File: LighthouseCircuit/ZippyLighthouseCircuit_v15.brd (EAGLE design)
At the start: 25.4 x 8.9 mm, 23 parts

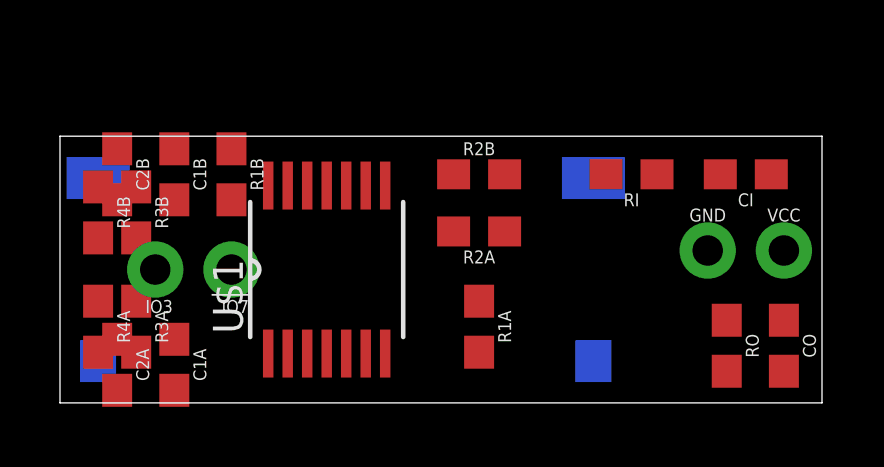
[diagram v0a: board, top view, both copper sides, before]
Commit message: Significant changes and refactored codebase layout. Improvements made to path following, PID control, path execution, added a new default path, and many other changes.
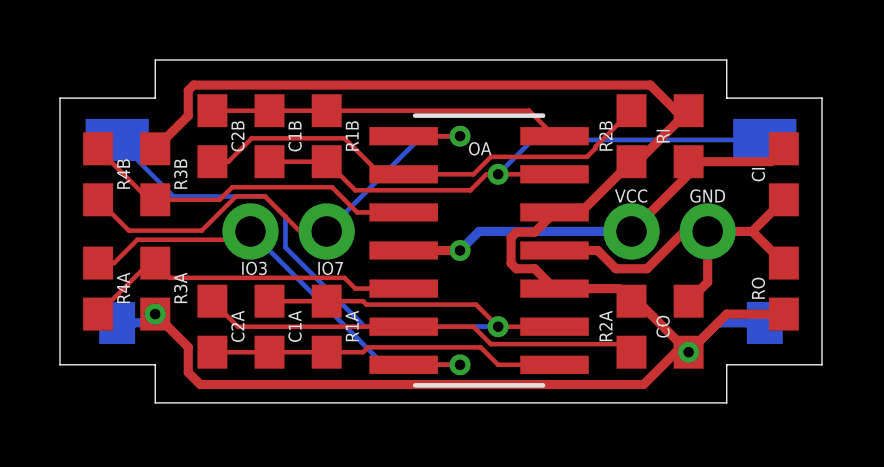
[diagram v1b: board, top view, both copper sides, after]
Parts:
- removed U$1: TLV2464IPW, ZippyComponentLibrary:PW14
- added OA: TLV2464IDM, ZippyComponentLibrary:D14-M
- moved R2A 5.99 mm to (19.1, 2.54), turned to 90 degrees
- moved D2 5.85 mm to (23.5, 5.71)
- moved R2B 5.24 mm to (19.1, 8.89), turned to 270 degrees
- moved VCC 5.12 mm to (19.1, 5.71)
- moved R1A 5.08 mm to (8.89, 2.54)
- moved R1B 3.42 mm to (8.89, 8.89)
- moved C1B 3.42 mm to (6.99, 8.89)
- moved IO7 3.42 mm to (8.89, 5.71)
- moved C1A 3.42 mm to (6.99, 2.54)
- moved C2A 3.42 mm to (5.08, 2.54)
- moved C2B 3.42 mm to (5.08, 8.89)
- moved IO3 3.42 mm to (6.35, 5.71)
- moved CO 3.24 mm to (21.0, 2.54), turned to 90 degrees
- moved RO 2.69 mm to (24.1, 3.81), turned to 270 degrees
- moved RI 2.29 mm to (21.0, 8.89), turned to 270 degrees
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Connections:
- net D1IN: now also OA.13; no longer U$1.13
- net D1OA2P: now also OA.2; no longer U$1.2
- net D1OAOUT1: now also OA.14; no longer U$1.14
- net D2IN: now also OA.9; no longer U$1.9
- net D2OA1OUT: now also OA.8; no longer U$1.8
- net D2OA2N: now also OA.5; no longer U$1.5
- net D2OA2P: now also OA.6; no longer U$1.6
- net GND: now also OA.11; no longer U$1.11
- net IO3: now also OA.7; no longer U$1.7
- net IO7: now also OA.1; no longer U$1.1
- net LVCC: now also OA.10, OA.12; no longer U$1.10, U$1.12
- net N$11: now also OA.3; no longer U$1.3
- net VCC: now also OA.4; no longer U$1.4
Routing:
- net LVCC: track 0.00 -> 62.9 mm, vias 0 -> 2
- net D2IN: track 0.00 -> 25.7 mm, vias 0 -> 1
- net D1IN: track 0.00 -> 19.5 mm, vias 0 -> 1
- net IO7: track 0.00 -> 16.6 mm, vias 0 -> 1
- net IO3: track 0.00 -> 16.2 mm, vias 0 -> 1
- net D1OA2P: track 0.00 -> 15.7 mm
- net D2OA2P: track 0.00 -> 14.7 mm
- net VCC: track 0.00 -> 14.3 mm, vias 0 -> 1
- net GND: track 0.00 -> 12.9 mm
- net D1OAOUT1: track 0.00 -> 11.8 mm
- net D2OA1OUT: track 0.00 -> 11.7 mm
- net N$11: track 0.00 -> 11.4 mm
- net D2OA2N: track 0.00 -> 11.2 mm
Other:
- board size 25.4 x 8.9 mm -> 25.4 x 11.4 mm
- board text added: "v1.5"
